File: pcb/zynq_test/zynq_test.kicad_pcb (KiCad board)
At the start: 6 copper layers, 100 x 102 mm, 25 parts, among them J1002 USB_A, J1101 RJ45_JK0654219, J1201 1-1734248-5, J1202 1-1734248-5, J1204 1-1734248-5, J1401 Barrel_Jack, J1402 Conn_02x05_Odd_Even, J702 USB_B_Micro, J801 HDMI_A, J802 HDMI_A, J901 A-MicroTF-1.85A, Q1102 2N7002E, Q1103 2N7002E, Q1104 2N7002E, U1002 TUSB1210-Q1, U1003 AP22816AKBWT, U1102 LAN8830, U1405 74LVC1G17, U202 XC7Z020-2CLG400I, U401 MT41K256M16TW-107, U402 MT41K256M16TW-107, U702 FT2232HQ, U803 TDP1204RNQR, U806 TDP1204RNQR, U901 TXS02612RTW

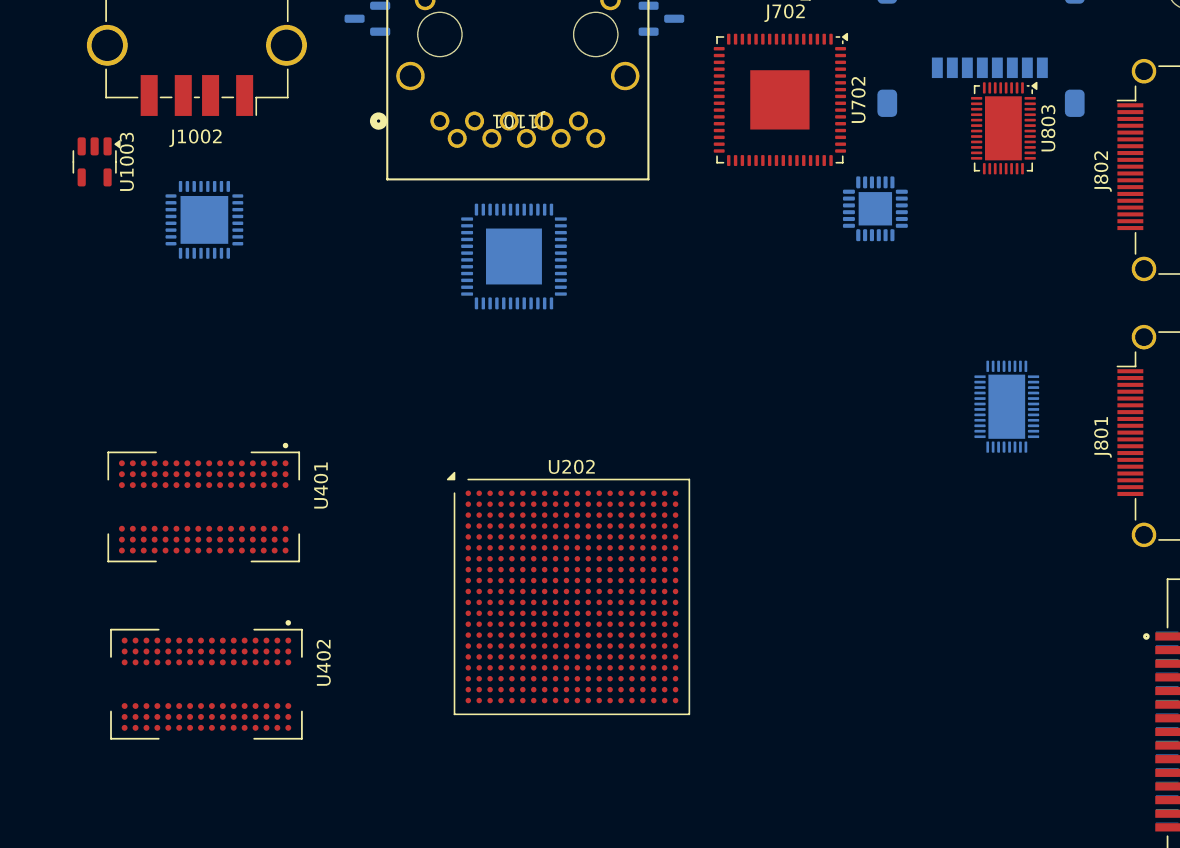
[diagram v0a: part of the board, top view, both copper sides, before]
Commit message: Finished to first ddr ic
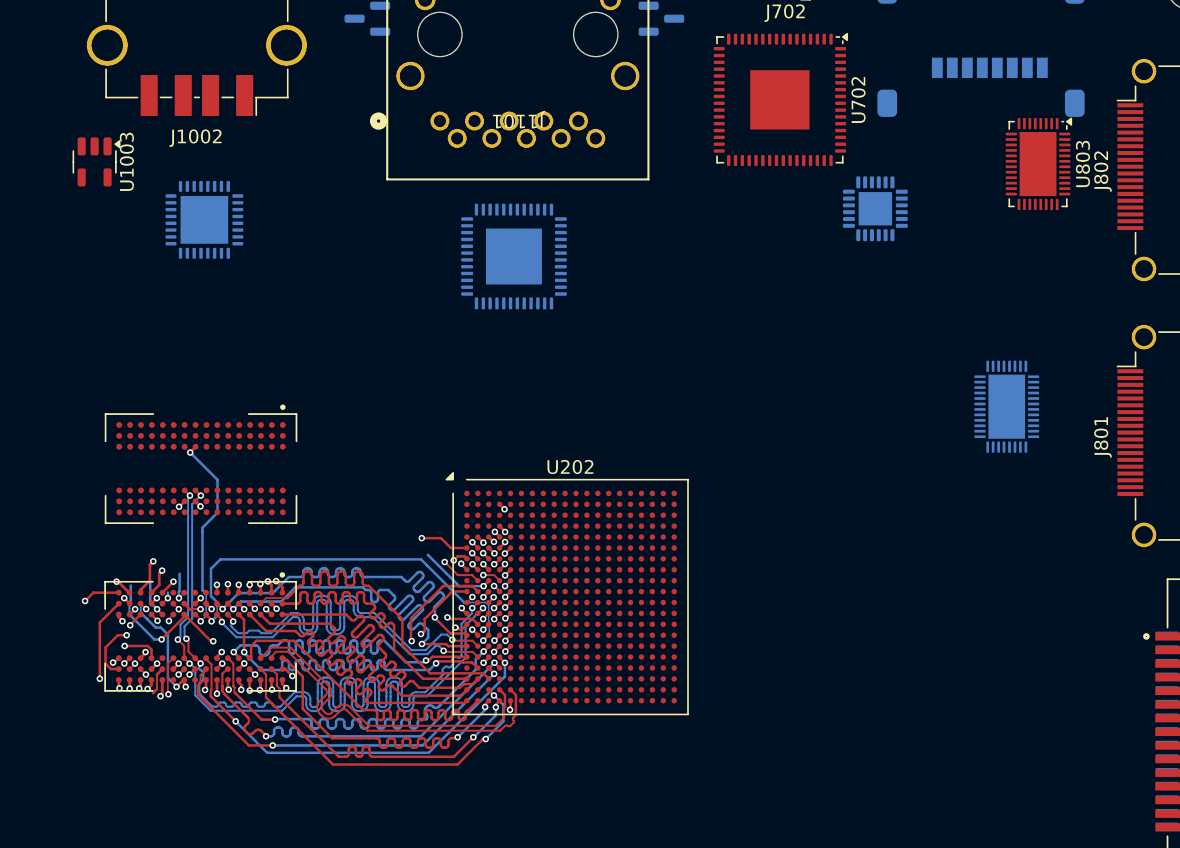
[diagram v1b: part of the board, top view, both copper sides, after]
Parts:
- U202: footprint Package_BGA:Xilinx_CLG400 -> Zynq:Zynq_Z7020-2CLG400I_W_Delay
- U401, U402: footprint dram:BGA96C80P9X16_1400X800X120 -> dram:BGA96C80P9X16_1400X800X120_pinDelays
- moved U803 3.65 mm to (163.2, 57.2)
- moved U402 3.54 mm to (101.8, 91.8)
- moved U401 2.82 mm to (101.8, 79.5)
- moved U202 0.10 mm to (128.9, 88.9)
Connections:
- U401 pad A2: /Zynq Dram/DDR_L1.13 -> /Zynq Dram/DDR_L0.1
- U401 pad A3: /Zynq Dram/DDR_L1.15 -> /Zynq Dram/DDR_L0.2
- U401 pad A7: /Zynq Dram/DDR_L1.12 -> /Zynq Dram/DDR_L0.6
- U401 pad B7: /Zynq Dram/DDR_L1.DQS_N -> /Zynq Dram/DDR_L0.DQS_N
- U401 pad B8: /Zynq Dram/DDR_L1.14 -> /Zynq Dram/DDR_L0.4
- U401 pad C2: /Zynq Dram/DDR_L1.11 -> /Zynq Dram/DDR_L0.3
- U401 pad C3: /Zynq Dram/DDR_L1.9 -> /Zynq Dram/DDR_L0.0
- U401 pad C7: /Zynq Dram/DDR_L1.DQS_P -> /Zynq Dram/DDR_L0.DQS_P
- U401 pad C8: /Zynq Dram/DDR_L1.10 -> /Zynq Dram/DDR_L0.5
- U401 pad D3: /Zynq Dram/DDR_L1.DM -> /Zynq Dram/DDR_L0.DM
- U401 pad D7: /Zynq Dram/DDR_L1.8 -> /Zynq Dram/DDR_L0.7
- U401 pad E3: /Zynq Dram/DDR_L0.0 -> /Zynq Dram/DDR_L1.8
- U401 pad E7: /Zynq Dram/DDR_L0.DM -> /Zynq Dram/DDR_L1.DM
- U401 pad F2: /Zynq Dram/DDR_L0.2 -> /Zynq Dram/DDR_L1.9
- U401 pad F3: /Zynq Dram/DDR_L0.DQS_P -> /Zynq Dram/DDR_L1.DQS_P
- U401 pad F7: /Zynq Dram/DDR_L0.1 -> /Zynq Dram/DDR_L1.15
- U401 pad F8: /Zynq Dram/DDR_L0.3 -> /Zynq Dram/DDR_L1.13
- U401 pad G2: /Zynq Dram/DDR_L0.6 -> /Zynq Dram/DDR_L1.10
- U401 pad G3: /Zynq Dram/DDR_L0.DQS_N -> /Zynq Dram/DDR_L1.DQS_N
- U401 pad H3: /Zynq Dram/DDR_L0.4 -> /Zynq Dram/DDR_L1.14
- U401 pad H7: /Zynq Dram/DDR_L0.7 -> /Zynq Dram/DDR_L1.11
- U401 pad H8: /Zynq Dram/DDR_L0.5 -> /Zynq Dram/DDR_L1.12
- U402 pad A2: /Zynq Dram/DDR_L3.29 -> /Zynq Dram/DDR_L3.24
- U402 pad A3: /Zynq Dram/DDR_L3.31 -> /Zynq Dram/DDR_L3.30
- U402 pad A7: /Zynq Dram/DDR_L3.28 -> /Zynq Dram/DDR_L3.25
- U402 pad B8: /Zynq Dram/DDR_L3.30 -> /Zynq Dram/DDR_L3.27
- U402 pad C2: /Zynq Dram/DDR_L3.27 -> /Zynq Dram/DDR_L3.31
- U402 pad C3: /Zynq Dram/DDR_L3.25 -> /Zynq Dram/DDR_L3.26
- U402 pad C8: /Zynq Dram/DDR_L3.26 -> /Zynq Dram/DDR_L3.29
- U402 pad D7: /Zynq Dram/DDR_L3.24 -> /Zynq Dram/DDR_L3.28
- U402 pad E3: /Zynq Dram/DDR_L2.16 -> /Zynq Dram/DDR_L2.22
- U402 pad F2: /Zynq Dram/DDR_L2.18 -> /Zynq Dram/DDR_L2.19
- U402 pad F7: /Zynq Dram/DDR_L2.17 -> /Zynq Dram/DDR_L2.18
- U402 pad F8: /Zynq Dram/DDR_L2.19 -> /Zynq Dram/DDR_L2.21
- U402 pad G2: /Zynq Dram/DDR_L2.22 -> /Zynq Dram/DDR_L2.16
- U402 pad H3: /Zynq Dram/DDR_L2.20 -> /Zynq Dram/DDR_L2.17
- U402 pad H7: /Zynq Dram/DDR_L2.23 -> /Zynq Dram/DDR_L2.20
- U402 pad H8: /Zynq Dram/DDR_L2.21 -> /Zynq Dram/DDR_L2.23
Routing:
- net /Zynq Dram/DDR_CTR.CLK_P: track 0.00 -> 60.2 mm, vias 0 -> 4
- net /Zynq Dram/DDR_CTR.CLK_N: track 0.00 -> 59.0 mm, vias 0 -> 4
- net /Zynq Dram/DDR_CTR.CLK_E: track 0.00 -> 53.4 mm, vias 0 -> 3
- net /Zynq Dram/DDR_CTR.RAS: track 0.00 -> 53.4 mm, vias 0 -> 3
- net /Zynq Dram/DDR_CTR.CAS: track 0.00 -> 50.9 mm, vias 0 -> 3
- net /Zynq Dram/DDR_CTR.RST: track 0.00 -> 50.9 mm, vias 0 -> 2
- net /Zynq Dram/DDR_CTR.BA0: track 0.00 -> 45.0 mm, vias 0 -> 2
- net /Zynq Dram/DDR_CTR.ODT: track 0.00 -> 44.0 mm, vias 0 -> 2
- net /Zynq Dram/DDR_CTR.BA2: track 0.00 -> 43.6 mm, vias 0 -> 2
- net /Zynq Dram/DDR_CTR.CS: track 0.00 -> 43.4 mm, vias 0 -> 2
- net /Zynq Dram/DDR_ADDR3: track 0.00 -> 43.1 mm, vias 0 -> 2
- net /Zynq Dram/DDR_ADDR1: track 0.00 -> 42.9 mm, vias 0 -> 2
- net /Zynq Dram/DDR_ADDR2: track 0.00 -> 42.1 mm, vias 0 -> 2
- net /Zynq Dram/DDR_ADDR5: track 0.00 -> 42.0 mm, vias 0 -> 2
- net /Zynq Dram/DDR_ADDR11: track 0.00 -> 42.0 mm, vias 0 -> 2
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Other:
- copper layers 6 -> 8

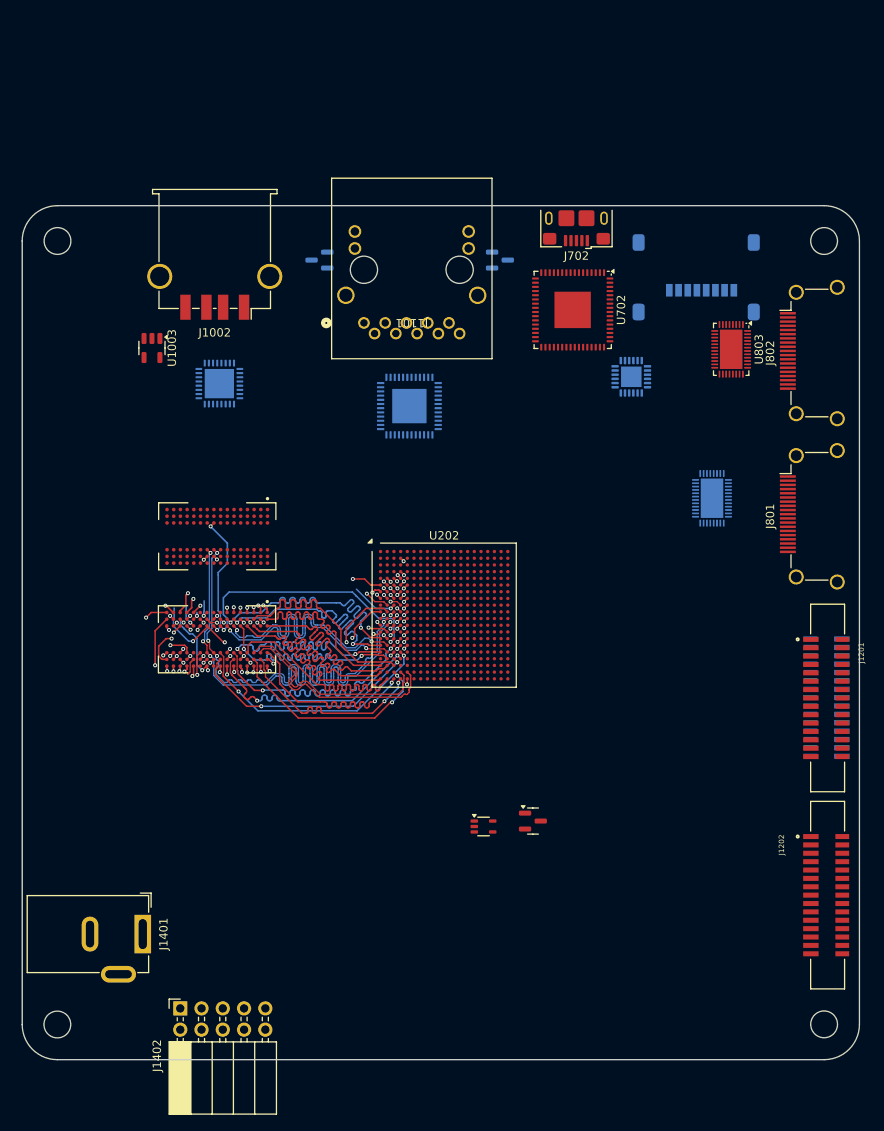
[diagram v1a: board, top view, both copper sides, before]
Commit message: DDR routed
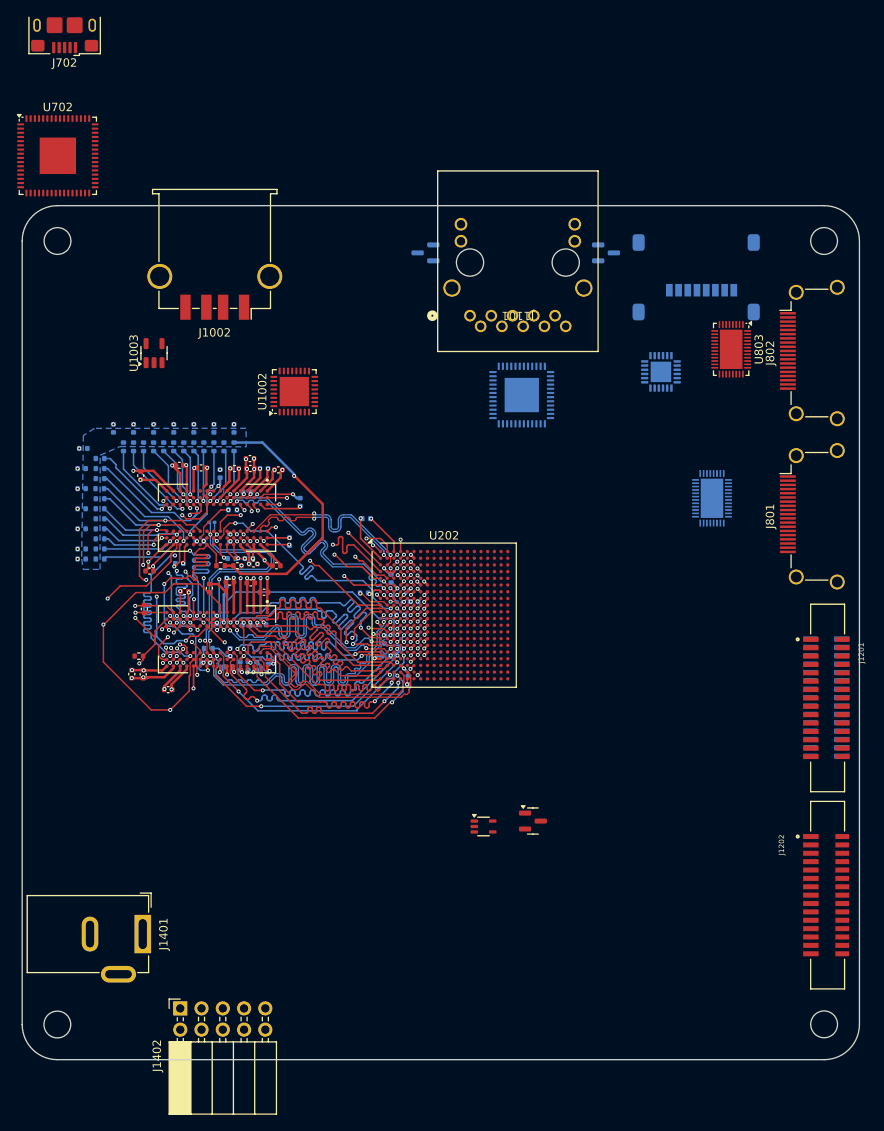
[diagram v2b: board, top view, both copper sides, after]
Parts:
- added C401: 470n, Capacitor_SMD:C_0402_1005Metric, B.Cu at (125.3, 87.3)
- added C402: 4u7, Capacitor_SMD:C_0402_1005Metric, B.Cu at (89.4, 66.6)
- added C403: 470n, Capacitor_SMD:C_0402_1005Metric, B.Cu at (85.6, 73.8)
- added C404: 100n, Capacitor_SMD:C_0402_1005Metric, B.Cu at (85.8, 69.0)
- added C405: 4u7, Capacitor_SMD:C_0402_1005Metric, B.Cu at (91.8, 66.6)
- added C406: 470n, Capacitor_SMD:C_0402_1005Metric, F.Cu at (104.2, 83.0)
- added C407: 100n, Capacitor_SMD:C_0402_1005Metric, B.Cu at (85.6, 76.2)
- added C408: 4u7, Capacitor_SMD:C_0402_1005Metric, B.Cu at (85.6, 78.6)
- added C409: 470n, Capacitor_SMD:C_0402_1005Metric, B.Cu at (85.6, 82.2)
- added C410: 100n, Capacitor_SMD:C_0402_1005Metric, B.Cu at (85.6, 71.4)
- added C411: 470n, Capacitor_SMD:C_0402_1005Metric, B.Cu at (101.4, 66.6)
- added C412: 4u7, Capacitor_SMD:C_0402_1005Metric, B.Cu at (99.0, 66.6)
- added C413: 100n, Capacitor_SMD:C_0402_1005Metric, B.Cu at (103.8, 66.6)
- added C414: 100n, Capacitor_SMD:C_0402_1005Metric, B.Cu at (85.6, 81.0)
- added C415: 4u7, Capacitor_SMD:C_0402_1005Metric, B.Cu at (94.2, 66.6)
- added C416: 4u7, Capacitor_SMD:C_0402_1005Metric, B.Cu at (96.6, 66.6)
- added C501: 470n, Capacitor_SMD:C_0402_1005Metric, F.Cu at (105.8, 85.0)
- added C502: 470n, Capacitor_SMD:C_0402_1005Metric, B.Cu at (111.7, 75.4)
- added C503: 47n, Capacitor_SMD:C_0402_1005Metric, B.Cu at (102.9, 85.0)
- added C504: 47n, Capacitor_SMD:C_0402_1005Metric, F.Cu at (93.7, 83.6)
- added C505: 47n, Capacitor_SMD:C_0402_1005Metric, B.Cu at (103.1, 95.1)
- added C506: 47n, Capacitor_SMD:C_0402_1005Metric, B.Cu at (105.3, 74.2)
- added C507: 47n, Capacitor_SMD:C_0402_1005Metric, B.Cu at (106.5, 95.0)
- added C508: 47n, Capacitor_SMD:C_0402_1005Metric, F.Cu at (105.8, 71.4)
- added C509: 47n, Capacitor_SMD:C_0402_1005Metric, B.Cu at (104.5, 95.0)
- added C510: 47n, Capacitor_SMD:C_0402_1005Metric, B.Cu at (107.4, 71.4)
- added C511: 47n, Capacitor_SMD:C_0402_1005Metric, F.Cu at (103.3, 85.0)
- added C512: 47n, Capacitor_SMD:C_0402_1005Metric, B.Cu at (97.3, 82.7)
- added C513: 47n, Capacitor_SMD:C_0402_1005Metric, B.Cu at (101.7, 89.5)
- added C514: 47n, Capacitor_SMD:C_0402_1005Metric, B.Cu at (103.3, 79.7)
- added C515: 47n, Capacitor_SMD:C_0402_1005Metric, B.Cu at (103.3, 93.3)
- added C516: 47n, Capacitor_SMD:C_0402_1005Metric, F.Cu at (106.1, 82.8)
- added C517: 47n, Capacitor_SMD:C_0402_1005Metric, B.Cu at (107.9, 95.2)
- added C518: 47n, Capacitor_SMD:C_0402_1005Metric, F.Cu at (109.1, 71.6)
- added C519: 47n, Capacitor_SMD:C_0402_1005Metric, F.Cu at (99.9, 71.3)
- added C520: 47n, Capacitor_SMD:C_0402_1005Metric, B.Cu at (105.5, 94.9)
- added C521: 47n, Capacitor_SMD:C_0402_1005Metric, B.Cu at (105.6, 82.2)
- added C522: 47n, Capacitor_SMD:C_0402_1005Metric, F.Cu at (97.9, 86.1)
- added C523: 47n, Capacitor_SMD:C_0402_1005Metric, B.Cu at (99.7, 80.1)
- added C524: 47n, Capacitor_SMD:C_0402_1005Metric, B.Cu at (100.4, 94.6)
- added C525: 47n, Capacitor_SMD:C_0402_1005Metric, F.Cu at (108.9, 83.0)
- added C526: 47n, Capacitor_SMD:C_0402_1005Metric, B.Cu at (107.2, 90.0)
- added C527: 47n, Capacitor_SMD:C_0402_1005Metric, F.Cu at (92.7, 72.2)
- added C528: 47n, Capacitor_SMD:C_0402_1005Metric, B.Cu at (105.3, 90.1)
- added C529: 10n, Capacitor_SMD:C_0402_1005Metric, F.Cu at (100.9, 85.7)
- added C530: 47n, Capacitor_SMD:C_0402_1005Metric, F.Cu at (97.3, 71.0)
- added C531: 10n, Capacitor_SMD:C_0402_1005Metric, B.Cu at (102.1, 72.0)
- added C532: 47n, Capacitor_SMD:C_0402_1005Metric, F.Cu at (95.9, 97.8)
- added C533: 47n, Capacitor_SMD:C_0402_1005Metric, B.Cu at (110.4, 80.1)
- added C534: 47n, Capacitor_SMD:C_0402_1005Metric, F.Cu at (93.0, 96.0)
- added C535: 47n, Capacitor_SMD:C_0402_1005Metric, B.Cu at (103.5, 82.2)
- added C536: 47n, Capacitor_SMD:C_0402_1005Metric, F.Cu at (93.1, 88.2)
- added C537: 470n, Capacitor_SMD:C_0402_1005Metric, F.Cu at (103.9, 71.4)
- added C538: 470n, Capacitor_SMD:C_0402_1005Metric, F.Cu at (107.4, 86.2)
- added C539: 4u7, Capacitor_SMD:C_0402_1005Metric, F.Cu at (105.7, 70.2)
- added C540: 4u7, Capacitor_SMD:C_0402_1005Metric, F.Cu at (91.6, 96.0)
- added C617: 470n, Capacitor_SMD:C_0402_1005Metric, B.Cu at (119.3, 86.3)
- added C620: 470n, Capacitor_SMD:C_0402_1005Metric, B.Cu at (124.6, 96.7)
- added C622: 470n, Capacitor_SMD:C_0402_1005Metric, B.Cu at (122.6, 84.5)
- added C624: 470n, Capacitor_SMD:C_0402_1005Metric, B.Cu at (123.7, 88.9)
- added C627: 4u7, Capacitor_SMD:C_0402_1005Metric, B.Cu at (121.8, 91.8)
- added C630: 4u7, Capacitor_SMD:C_0402_1005Metric, B.Cu at (122.0, 93.8)
- added C632: 100u, Capacitor_SMD:C_0402_1005Metric, B.Cu at (119.6, 77.4)
- added R401: 80R, Resistor_SMD:R_0201_0603Metric, B.Cu at (124.5, 86.1)
- added R402: 80R, Resistor_SMD:R_0201_0603Metric, B.Cu at (123.6, 87.3)
- added R403: 4k7, Resistor_SMD:R_0402_1005Metric, F.Cu at (92.4, 93.8)
- added R404: 240R, Resistor_SMD:R_0402_1005Metric, B.Cu at (103.6, 76.3)
- added R405: 240R, Resistor_SMD:R_0402_1005Metric, B.Cu at (100.7, 92.9)
- added R406: 80R, Resistor_SMD:R_0201_0603Metric, B.Cu at (101.2, 77.8)
- added R407: 40R, Resistor_SMD:R_0402_1005Metric, B.Cu at (96.6, 68.8)
- added R408: 40R, Resistor_SMD:R_0402_1005Metric, B.Cu at (87.8, 78.6)
- added R409: 40R, Resistor_SMD:R_0402_1005Metric, B.Cu at (87.8, 77.4)
- added R410: 40R, Resistor_SMD:R_0402_1005Metric, B.Cu at (90.6, 68.8)
- added R411: 40R, Resistor_SMD:R_0402_1005Metric, F.Cu at (102.2, 83.0)
- added R412: 40R, Resistor_SMD:R_0402_1005Metric, B.Cu at (91.8, 68.8)
- added R413: 40R, Resistor_SMD:R_0402_1005Metric, B.Cu at (87.8, 73.8)
- added R414: 40R, Resistor_SMD:R_0402_1005Metric, B.Cu at (102.6, 68.8)
- added R415: 40R, Resistor_SMD:R_0402_1005Metric, B.Cu at (95.4, 68.8)
- added R416: 40R, Resistor_SMD:R_0402_1005Metric, B.Cu at (87.8, 79.8)
- added R417: 40R, Resistor_SMD:R_0402_1005Metric, B.Cu at (100.2, 68.8)
- added R418: 40R, Resistor_SMD:R_0402_1005Metric, B.Cu at (87.8, 82.2)
- added R419: 40R, Resistor_SMD:R_0402_1005Metric, B.Cu at (87.8, 75.0)
- added R420: 40R, Resistor_SMD:R_0402_1005Metric, B.Cu at (101.4, 68.8)
- added R421: 40R, Resistor_SMD:R_0402_1005Metric, B.Cu at (94.2, 68.8)
- added R422: 40R, Resistor_SMD:R_0402_1005Metric, B.Cu at (87.8, 70.2)
- added R423: 40R, Resistor_SMD:R_0402_1005Metric, B.Cu at (103.8, 68.8)
- added R424: 40R, Resistor_SMD:R_0402_1005Metric, B.Cu at (87.8, 81.0)
- added R425: 40R, Resistor_SMD:R_0402_1005Metric, B.Cu at (87.8, 76.2)
- added R426: 40R, Resistor_SMD:R_0402_1005Metric, B.Cu at (99.0, 68.8)
- added R427: 40R, Resistor_SMD:R_0402_1005Metric, B.Cu at (93.0, 68.8)
- added R428: 40R, Resistor_SMD:R_0402_1005Metric, B.Cu at (97.8, 68.8)
- added R429: 40R, Resistor_SMD:R_0402_1005Metric, B.Cu at (87.8, 72.6)
- added R430: 40R, Resistor_SMD:R_0402_1005Metric, B.Cu at (87.8, 71.4)
- U1002: moved to F.Cu
- moved J702 65.3 mm to (83.6, 18.4)
- moved U702 64.2 mm to (82.8, 34.0), turned to 0 degrees
- moved U1102 13.5 mm to (138.2, 62.6)
- moved J1101 12.7 mm to (132.0, 53.1)
- moved Q1103 12.7 mm to (126.7, 45.6)
- moved Q1102 12.7 mm to (148.2, 45.6)
- moved U1002 9.00 mm to (111.0, 62.2)
- moved U901 3.59 mm to (154.8, 59.9)
- moved U401 2.21 mm to (101.8, 77.3)
- moved U1003 0.66 mm to (94.2, 57.6), turned to 90 degrees
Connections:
- U401 pad A7: /Zynq Dram/DDR_L0.6 -> /Zynq Dram/DDR_L0.5
- U401 pad C3: /Zynq Dram/DDR_L0.0 -> /Zynq Dram/DDR_L0.6
- U401 pad C8: /Zynq Dram/DDR_L0.5 -> /Zynq Dram/DDR_L0.7
- U401 pad D7: /Zynq Dram/DDR_L0.7 -> /Zynq Dram/DDR_L0.0
- U401 pad E3: /Zynq Dram/DDR_L1.8 -> /Zynq Dram/DDR_L1.11
- U401 pad F2: /Zynq Dram/DDR_L1.9 -> /Zynq Dram/DDR_L1.10
- U401 pad F7: /Zynq Dram/DDR_L1.15 -> /Zynq Dram/DDR_L1.13
- U401 pad F8: /Zynq Dram/DDR_L1.13 -> /Zynq Dram/DDR_L1.14
- U401 pad G2: /Zynq Dram/DDR_L1.10 -> /Zynq Dram/DDR_L1.9
- U401 pad H3: /Zynq Dram/DDR_L1.14 -> /Zynq Dram/DDR_L1.8
- U401 pad H7: /Zynq Dram/DDR_L1.11 -> /Zynq Dram/DDR_L1.15
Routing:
- net V_{TT 0.675} REF: track 2.06 -> 121.4 mm, vias 0 -> 6
- net GND: track 25.5 -> 133.0 mm, vias 28 -> 82
- net +1V35: track 19.2 -> 115.4 mm, vias 24 -> 48
- net /Zynq Dram/DDR_CTR.BA1: track 36.8 -> 78.4 mm, vias 2 -> 4
- net /Zynq Dram/DDR_CTR.BA2: track 43.6 -> 84.9 mm, vias 2 -> 4
- net /Zynq Dram/DDR_ADDR10: track 41.5 -> 78.5 mm, vias 2 -> 5
- net /Zynq Dram/DDR_ADDR4: track 37.3 -> 73.9 mm, vias 2 -> 5
- net /Zynq Dram/DDR_ADDR2: track 42.1 -> 78.3 mm, vias 2 -> 3
- net /Zynq Dram/DDR_ADDR13: track 37.6 -> 73.2 mm, vias 2 -> 4
- net /Zynq Dram/DDR_ADDR9: track 40.5 -> 75.9 mm, vias 2 -> 4
- net /Zynq Dram/DDR_ADDR1: track 42.9 -> 77.9 mm, vias 2 -> 4
- net /Zynq Dram/DDR_ADDR12: track 39.0 -> 73.6 mm, vias 2 -> 4
- net /Zynq Dram/DDR_ADDR8: track 42.0 -> 76.2 mm, vias 2 -> 4
- net /Zynq Dram/DDR_ADDR0: track 41.1 -> 75.1 mm, vias 2 -> 3
- net /Zynq Dram/DDR_CTR.WE: track 38.1 -> 71.9 mm, vias 2 -> 5
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- added copper zone on In2.Cu, net +1V35
- added copper zone on B.Cu, net +V_{TT} 0V675
- added copper zone on B.Cu, net GND
